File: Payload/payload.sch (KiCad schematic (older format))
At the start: 40 parts

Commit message: Testpoints, specific values, CE, series protection, crystal, headers.
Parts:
- removed J?: Conn_02x20_Odd_Even, symbol Connector_Generic:Conn_02x20_Odd_Even
- removed R? (x16): R_Small_US, symbol Device:R_Small_US
- removed U?: LTC1153IS8-PBF, SOIC-8_S_LIT, symbol Payload2:LTC1153IS8-PBF
- added C? (x3): 100 nF, symbol Device:C_Small
- added C? (x2): C_Small, symbol Device:C_Small
- added C?: 1 uF, symbol Device:C_Small
- added J?: Conn_02x02_Odd_Even, symbol Connector_Generic:Conn_02x02_Odd_Even
- added J?: Conn_02x03_Odd_Even, symbol Connector_Generic:Conn_02x03_Odd_Even
- added Q?: Q_PMOS_DGS, symbol Device:Q_PMOS_DGS
- added R? (x2): 10 kR, symbol Device:R_Small_US
- added R? (x2): R_Small_US, symbol Device:R_Small_US
- added R?: 1 kR, symbol Device:R_Small_US
- added R? (x3): 100 kR, symbol Device:R_Small_US
- added R? (x7): 200 R, symbol Device:R_Small_US
- added R?: 55 R, symbol Device:R_Small_US
- added TP? (x37): TestPoint, symbol Connector:TestPoint
- added U? (x3): CY62167EV30LL-45ZXA, TSOP-48, symbol Payload2:CY62167EV30LL-45ZXA
- added Y?: 8 MHz, symbol Device:Crystal_GND24_Small
- C?: value C_Small -> 100 nF
- C?: value 100 nF -> 10 nF
- R? (x3): value R_Small_US -> 200 R
- R? (x3): value R_Small_US -> 10 kR
- R?: value R_Small_US -> 100 kR
- R?: value R_Small_US -> 1 kR
- R?: value R_Small_US -> 100 K
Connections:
- net A0: now also TP?.1, U?.25 (A0), U?.25 (A0), U?.25 (A0)
- net A1: now also TP?.1, U?.24 (A1), U?.24 (A1), U?.24 (A1)
- net A10: now also U?.57 (PB5), TP?.1, U?.6 (A10), U?.6 (A10), U?.6 (A10); no longer U?.28 (PB2)
- net A11: now also U?.58 (PB6), TP?.1, U?.5 (A11), U?.5 (A11), U?.5 (A11); no longer U?.55 (PB3)
- net A12: now also U?.59 (PB7), TP?.1, U?.4 (A12), U?.4 (A12), U?.4 (A12); no longer U?.56 (PB4)
- net A13: now also U?.61 (PB8), TP?.1, U?.3 (A13), U?.3 (A13), U?.3 (A13); no longer U?.57 (PB5)
- net A14: now also U?.62 (PB9), TP?.1, U?.2 (A14), U?.2 (A14), U?.2 (A14); no longer U?.58 (PB6)
- net A15: now also U?.29 (PB10), TP?.1, U?.1 (A15), U?.1 (A15), U?.1 (A15); no longer U?.59 (PB7)
- net A16: now also U?.30 (PB11), TP?.1, U?.48 (A16), U?.48 (A16), U?.48 (A16); no longer U?.61 (PB8)
- net A17: now also U?.33 (PB12), TP?.1, U?.17 (A17), U?.17 (A17), U?.17 (A17); no longer U?.62 (PB9)
- net A18: now also U?.34 (PB13), TP?.1, U?.16 (A18), U?.16 (A18), U?.16 (A18); no longer U?.29 (PB10)
- net A19: now also U?.35 (PB14), TP?.1, U?.9 (A19), U?.9 (A19), U?.9 (A19); no longer U?.30 (PB11)
- net A2: now also TP?.1, U?.23 (A2), U?.23 (A2), U?.23 (A2)
- net A20: now also U?.36 (PB15), TP?.1, U?.45 (I/O15/A20), U?.45 (I/O15/A20), U?.45 (I/O15/A20); no longer U?.33 (PB12)
- net A3: now also TP?.1, U?.22 (A3), U?.22 (A3), U?.22 (A3)
- net A4: now also TP?.1, U?.21 (A4), U?.21 (A4), U?.21 (A4)
- net A5: now also U?.50 (PA15), TP?.1, U?.20 (A5), U?.20 (A5), U?.20 (A5); no longer U?.46 (PA13)
- net A6: now also U?.26 (PB0), TP?.1, U?.19 (A6), U?.19 (A6), U?.19 (A6); no longer U?.49 (PA14)
- net A7: now also U?.27 (PB1), TP?.1, U?.18 (A7), U?.18 (A7), U?.18 (A7); no longer U?.50 (PA15)
- net A8: now also U?.28 (PB2), TP?.1, U?.8 (A8), U?.8 (A8), U?.8 (A8); no longer U?.26 (PB0)
- net A9: now also U?.56 (PB4), TP?.1, U?.7 (A9), U?.7 (A9), U?.7 (A9); no longer U?.27 (PB1)
- net GND: now also C?.2, C?.1, C?.1, C?.1, C?.1, C?.2, C?.2, J?.4 (Pin_4), J?.6 (Pin_6), R?.2, R?.2, R?.2, TP?.1, U?.15 (*BLE), U?.15 (*BLE), U?.15 (*BLE), U?.26 (*CE1), U?.26 (*CE1), U?.26 (*CE1), U?.27 (VSS), U?.27 (VSS), U?.27 (VSS), U?.30 (I/O8), U?.30 (I/O8), U?.30 (I/O8), U?.32 (I/O9), U?.32 (I/O9), U?.32 (I/O9), U?.34 (I/O10), U?.34 (I/O10), U?.34 (I/O10), U?.36 (I/O11), U?.36 (I/O11), U?.36 (I/O11), U?.39 (I/O12), U?.39 (I/O12), U?.39 (I/O12), U?.41 (I/O13), U?.41 (I/O13), U?.41 (I/O13), U?.43 (I/O14), U?.43 (I/O14), U?.43 (I/O14), U?.46 (VSS), U?.46 (VSS), U?.46 (VSS), Y?.2, Y?.4; no longer C?.1, U?.5 (PH0), U?.6 (PH1)
- net I2C3_SCL: now also J?.1 (Pin_1)
- net I2C3_SDA: now also J?.3 (Pin_3)
- net IO0: now also TP?.1, U?.29 (I/O0), U?.29 (I/O0), U?.29 (I/O0)
- net IO1: now also R?.1, TP?.1, U?.31 (I/O1), U?.31 (I/O1), U?.31 (I/O1)
- net IO2: now also R?.1, TP?.1, U?.33 (I/O2), U?.33 (I/O2), U?.33 (I/O2)
- net IO3: now also R?.1, TP?.1, U?.35 (I/O3), U?.35 (I/O3), U?.35 (I/O3)
- net IO4: now also R?.1, TP?.1, U?.38 (I/O4), U?.38 (I/O4), U?.38 (I/O4)
- net IO5: now also R?.1, TP?.1, U?.40 (I/O5), U?.40 (I/O5), U?.40 (I/O5)
- net IO6: now also R?.1, TP?.1, U?.42 (I/O6), U?.42 (I/O6), U?.42 (I/O6)
- net IO7: now also R?.1, TP?.1, U?.44 (I/O7), U?.44 (I/O7), U?.44 (I/O7)
- net M1_CE: now also TP?.1
- net VCC: now also C?.2, J?.2 (Pin_2), J?.2 (Pin_2), Q?.3 (S), R?.1, R?.2, TP?.1
- net Vin: now also R?.2
- net ~OE: now also TP?.1, U?.28 (*OE), U?.28 (*OE), U?.28 (*OE)
- net ~WE: now also TP?.1, U?.11 (*WE), U?.11 (*WE), U?.11 (*WE)
- net at U?.15 (PA1): now also R?.2
- net at U?.16 (PA2): now also R?.2
- net at U?.17 (PA3): now also R?.2
- net at U?.20 (PA4): now also R?.2
- net at U?.21 (PA5): now also R?.2
- net at U?.22 (PA6): now also R?.2
- net at U?.23 (PA7): now also R?.2
- net at U?.24 (PC4): now also C?.2, R?.1, R?.2, U?.14 (*BHE), U?.37 (VCC), U?.47 (*BYTE), C?.2, C?.2, C?.2, R?.1, R?.1, R?.1, R?.2, U?.14 (*BHE), U?.14 (*BHE), U?.14 (*BHE), U?.37 (VCC), U?.37 (VCC), U?.37 (VCC), U?.47 (*BYTE), U?.47 (*BYTE), U?.47 (*BYTE)
- net at U?.25 (PC5): now also Q?.1 (D), R?.1, Q?.1 (D), R?.1
- net at R?.1: now also U?.37 (PC6), R?.1; no longer U?.34 (PB13)
- net M4_CE: now reaches U?.51 (PC10)
- net M4_CE: now also TP?.1, U?.12 (CE2)
- net M3_CE: now reaches U?.52 (PC11)
- net M3_CE: now also TP?.1, U?.12 (CE2)
- net M2_CE: now reaches U?.53 (PC12)
- net M2_CE: now also TP?.1, U?.12 (CE2)
- net at U?.60 (BOOT0): now also R?.2; no longer JP?.2 (B)
- net NRST: now reaches R?.2, U?.7 (NRST)
- net NRST: now also C?.1, SW?.2 (B), J?.4 (Pin_4); no longer C?.2
- net at R?.2, U?.8 (PC0): now also R?.2; no longer R?.2
- net at R?.2, U?.9 (PC1): now also R?.2; no longer R?.2
- net at Q?.2 (G), R?.2: now also Q?.2 (G), R?.1, R?.2
- new net: C?.1, U?.5 (PH0), Y?.1
- new net: R?.2, U?.6 (PH1)
- new net: JP?.2 (B), R?.1
- new net: C?.1, R?.1, Y?.3
- new net SWCLK: J?.3 (Pin_3), U?.49 (PA14)
- new net SWDIO: J?.1 (Pin_1), U?.46 (PA13)
- new net SWO: J?.5 (Pin_5), U?.55 (PB3)
- no-connect marks 0 -> 6
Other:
- note added: "TODO:\nAdd testpoints\nLayout optimization of pin assignments\nVerify that external supply connects to Vin, not Vcc\n\nNote:\nCant use BJT, too much drop\nWhen voltage at MCU is lower than drain, body diode conduction will equalize\nComparator checks resistor for quick cutoff if latched"
- note removed: "TODO:\nCheck cutoff freq of decoupling\nAdd programming header\nAdd testpoints\nLayout optimization of pin assignments\nCheck that external supply connects to Vin, not Vcc\nActually connect sense resistor pins for memory power\nto comparator pins\n\nNote:\nCant use BJT, too much drop\nWhen voltage at MCU is lower than drain, body diode conduction will equalize\nComparator checks resistor for quic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"
- moved on the sheet: C?, JP?, Q?, R?, SW?, U?

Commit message: Connectors, notes, general cleanup
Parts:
- removed C? (x3): 100 nF, symbol Device:C_Small
- removed J?: Conn_02x02_Odd_Even, symbol Connector_Generic:Conn_02x02_Odd_Even
- removed J?: Conn_02x03_Odd_Even, symbol Connector_Generic:Conn_02x03_Odd_Even
- removed R? (x2): 100 kR, symbol Device:R_Small_US
- removed R? (x2): 1 kR, symbol Device:R_Small_US
- added C? (x3): 100 nF, symbol Device:C_Small
- added J1: Conn_ARM_JTAG_SWD_10, symbol Connector:Conn_ARM_JTAG_SWD_10
- added J2: Conn_01x02, symbol Connector_Generic:Conn_01x02
- added J3: Conn_01x03, symbol Connector_Generic:Conn_01x03
- added R1, R4: 200 R, symbol Device:R_Small_US
- added R13: 100 K, symbol Device:R_Small_US
- gave numbers to parts that had none: 79
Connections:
- net GND: now also C?.1, C?.1, C?.1, J1.3 (GND), J1.5 (GND), J1.9 (GNDDetect), J2.2 (Pin_2), J3.3 (Pin_3), R13.2
- net I2C3_SCL: now also J3.1 (Pin_1), R1.1
- net I2C3_SDA: now also J3.2 (Pin_2), R4.1
- net NRST: now also J1.10 (~RESET~)
- net SWCLK: now also J1.4 (SWDCLK/TCK)
- net SWDIO: now also J1.2 (SWDIO/TMS)
- net SWO: now also J1.6 (SWO/TDO)
- net VCC: now also J1.1 (VTref), R13.1
- net at C9.2, R23.2, R24.2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: now also C?.2, C?.2, C?.2
- net at U1.37 (PC6): now also Q1.2 (G), Q2.2 (G), R22.1
- net at R2.2, R5.2, U1.8 (PC0): now also R1.2
- net at R3.2, R6.2, U1.9 (PC1): now also R4.2
- net Vin: no longer names the net of R7.2, R8.2
- net Vin: now also J2.1 (Pin_1)
- no-connect marks 6 -> 7
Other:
- note added: "Guarantees rail -> 0 within known time"
- note added: "Internal RC sufficient for operation,\nthis gains a few percent memory clock."
- note added: "TODO:\nConsider resistors on testpoints\nGeometrically optimize address and IO pin assignments\nVerify that external supply connects to Vin, not Vcc\nIf space permits double up IO resistors as well\n\nNotes:\n- Software: STM internal comparator -> sense resistor for quick cutoff if latched\n- Software: Can guaruntee rail -> 0 by sensing comparator low side, or switch GPIO to output and drive low.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"
- note added: "Text Template"
- note removed: "TODO:\nAdd testpoints\nLayout optimization of pin assignments\nVerify that external supply connects to Vin, not Vcc\n\nNote:\nCant use BJT, too much drop\nWhen voltage at MCU is lower than drain, body diode conduction will equalize\nComparator checks resistor for quick cutoff if latched"
- moved on the sheet: C1, C2, C3, C4, C5, C6, C7, C8, C9, JP1, Q1, Q2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

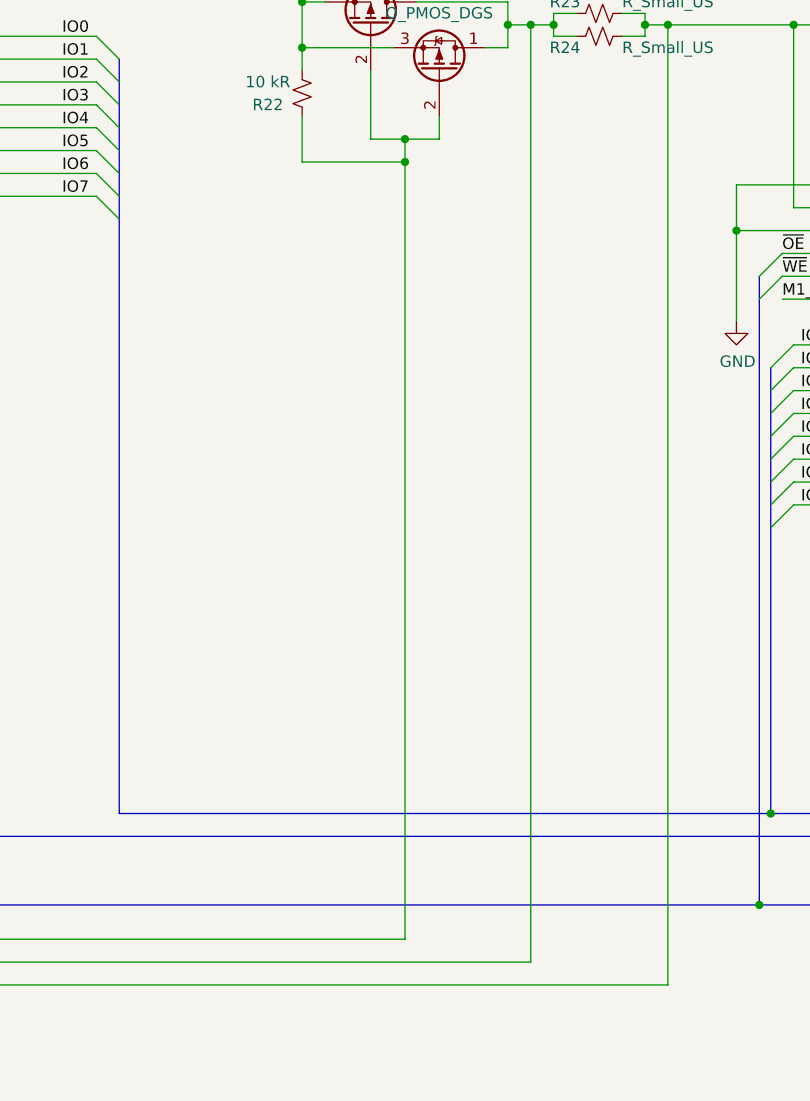
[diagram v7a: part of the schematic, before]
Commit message: Fix missing gate resistors
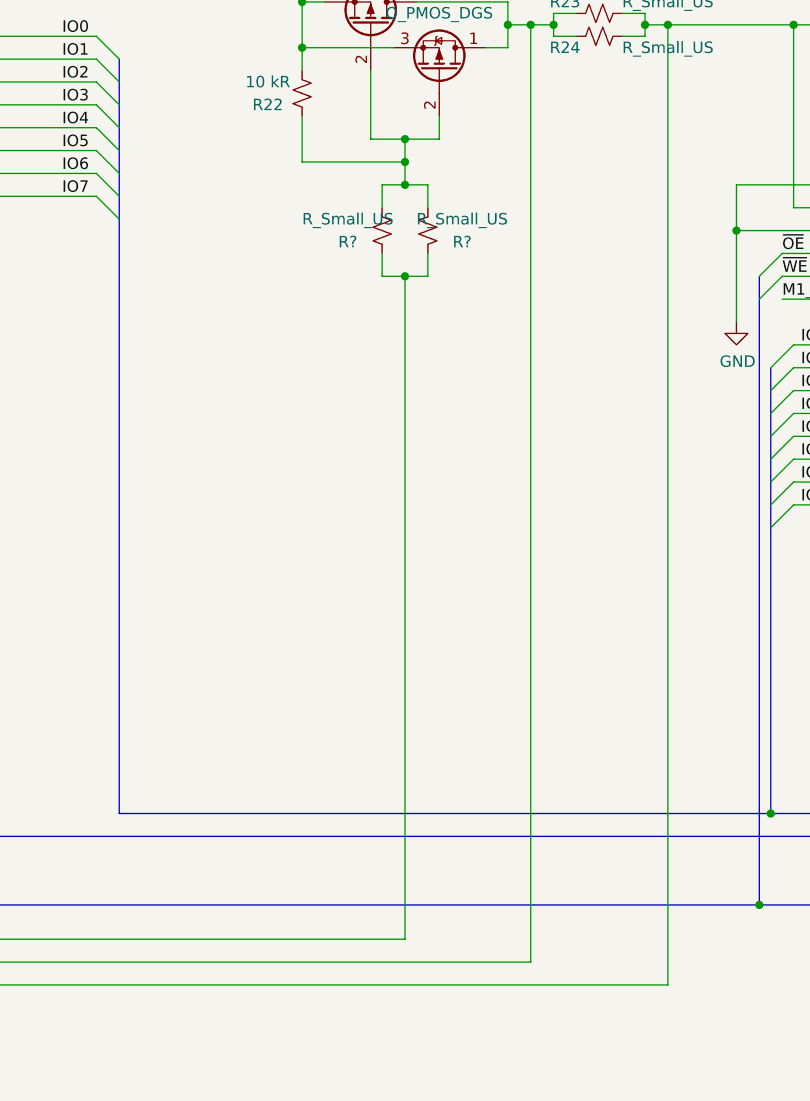
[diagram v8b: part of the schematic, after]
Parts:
- added R? (x2): R_Small_US, symbol Device:R_Small_US
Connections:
- net at Q1.2 (G), Q2.2 (G), R22.1: now also R?.2, R?.2; no longer U1.37 (PC6)
- new net: R?.1, R?.1, U1.37 (PC6)
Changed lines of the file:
@@
 Wire Wire Line
 	10750 13750 11050 13750
-Wire Wire Line
-	7550 4500 7550 7900
-Connection ~ 7550 4500
 $Comp
 L Device:R_Small_US R13
@@
 Wire Wire Line
 	4850 3500 5000 3500
+$Comp
+L Device:R_Small_US R?
+U 1 1 60735361
+P 7450 4800
+F 0 "R?" H 7600 4850 50  0000 C CNN
+F 1 "R_Small_US" H 7600 4750 50  0000 C CNN
+F 2 "" H 7450 4800 50  0001 C CNN
+F 3 "~" H 7450 4800 50  0001 C CNN
+	1    7450 4800
+	-1   0    0    1
+$EndComp
+Wire Wire Line
+	7450 4700 7450 4600
+Wire Wire Line
+	7450 4600 7550 4600
+Wire Wire Line
+	7550 4600 7550 4500
+Connection ~ 7550 4500
+Wire Wire Line
+	7550 4600 7650 4600
+Wire Wire Line
+	7650 4600 7650 4700
+Connection ~ 7550 4600
+$Comp
+L Device:R_Small_US R?
+U 1 1 6092031B
+P 7650 4800
+F 0 "R?" H 7800 4850 50  0000 C CNN
+F 1 "R_Small_US" H 7800 4750 50  0000 C CNN
+F 2 "" H 7650 4800 50  0001 C CNN
+F 3 "~" H 7650 4800 50  0001 C CNN
+	1    7650 4800
+	1    0    0    1
+$EndComp
+Wire Wire Line
+	7450 4900 7450 5000
+Wire Wire Line
+	7450 5000 7550 5000
+Wire Wire Line
+	7650 5000 7650 4900
+Wire Wire Line
+	7550 5000 7550 7900
 Wire Bus Line
 	18700 5000 18700 7750
@@
 Wire Bus Line
 	20750 4600 20750 7450
+Connection ~ 7550 5000
+Wire Wire Line
+	7550 5000 7650 5000
 $EndSCHEMATC
